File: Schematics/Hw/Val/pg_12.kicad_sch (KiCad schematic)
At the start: 19 parts, among them U1401 F04, U1402 F04, U1403 F04, U1404 F04, U1405 F04, U1406 F04, U1407 F04, U1408 F04, U1409 F04, U1410 F04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

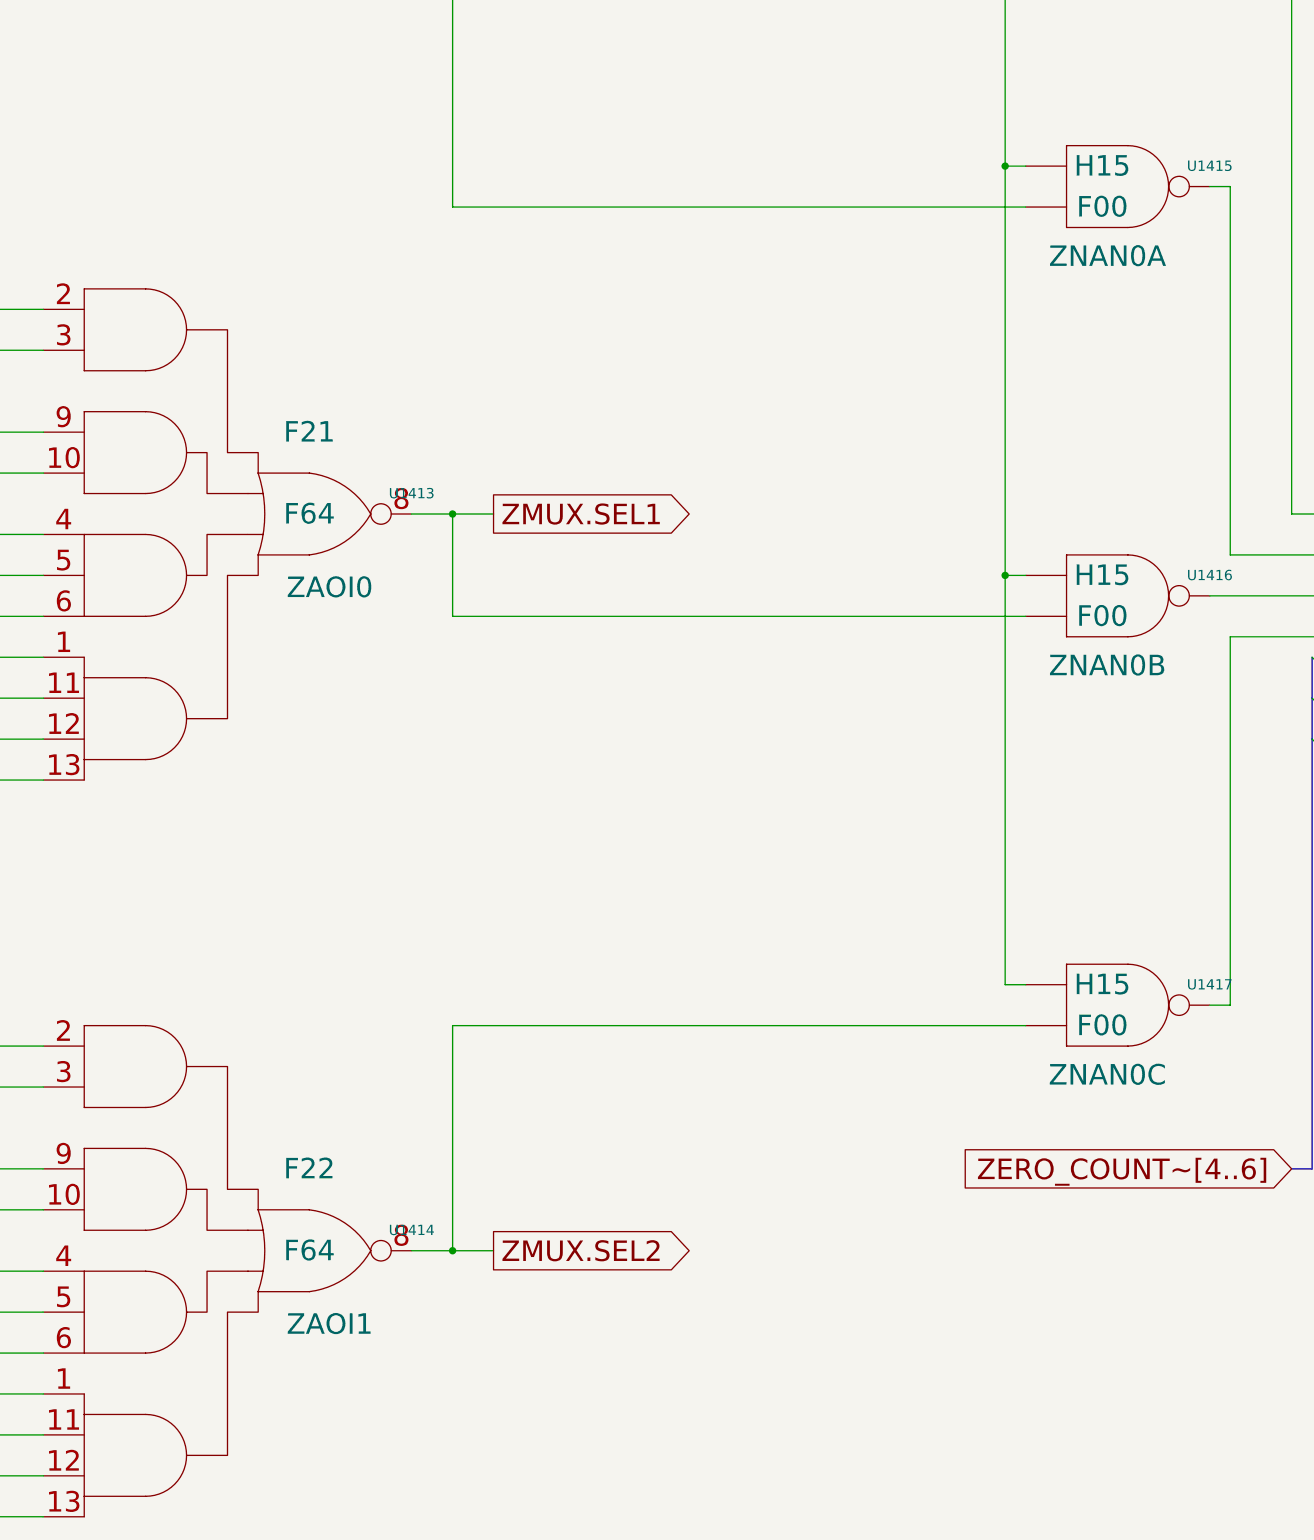
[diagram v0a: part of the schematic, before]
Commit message: Upgrade to KiCad9
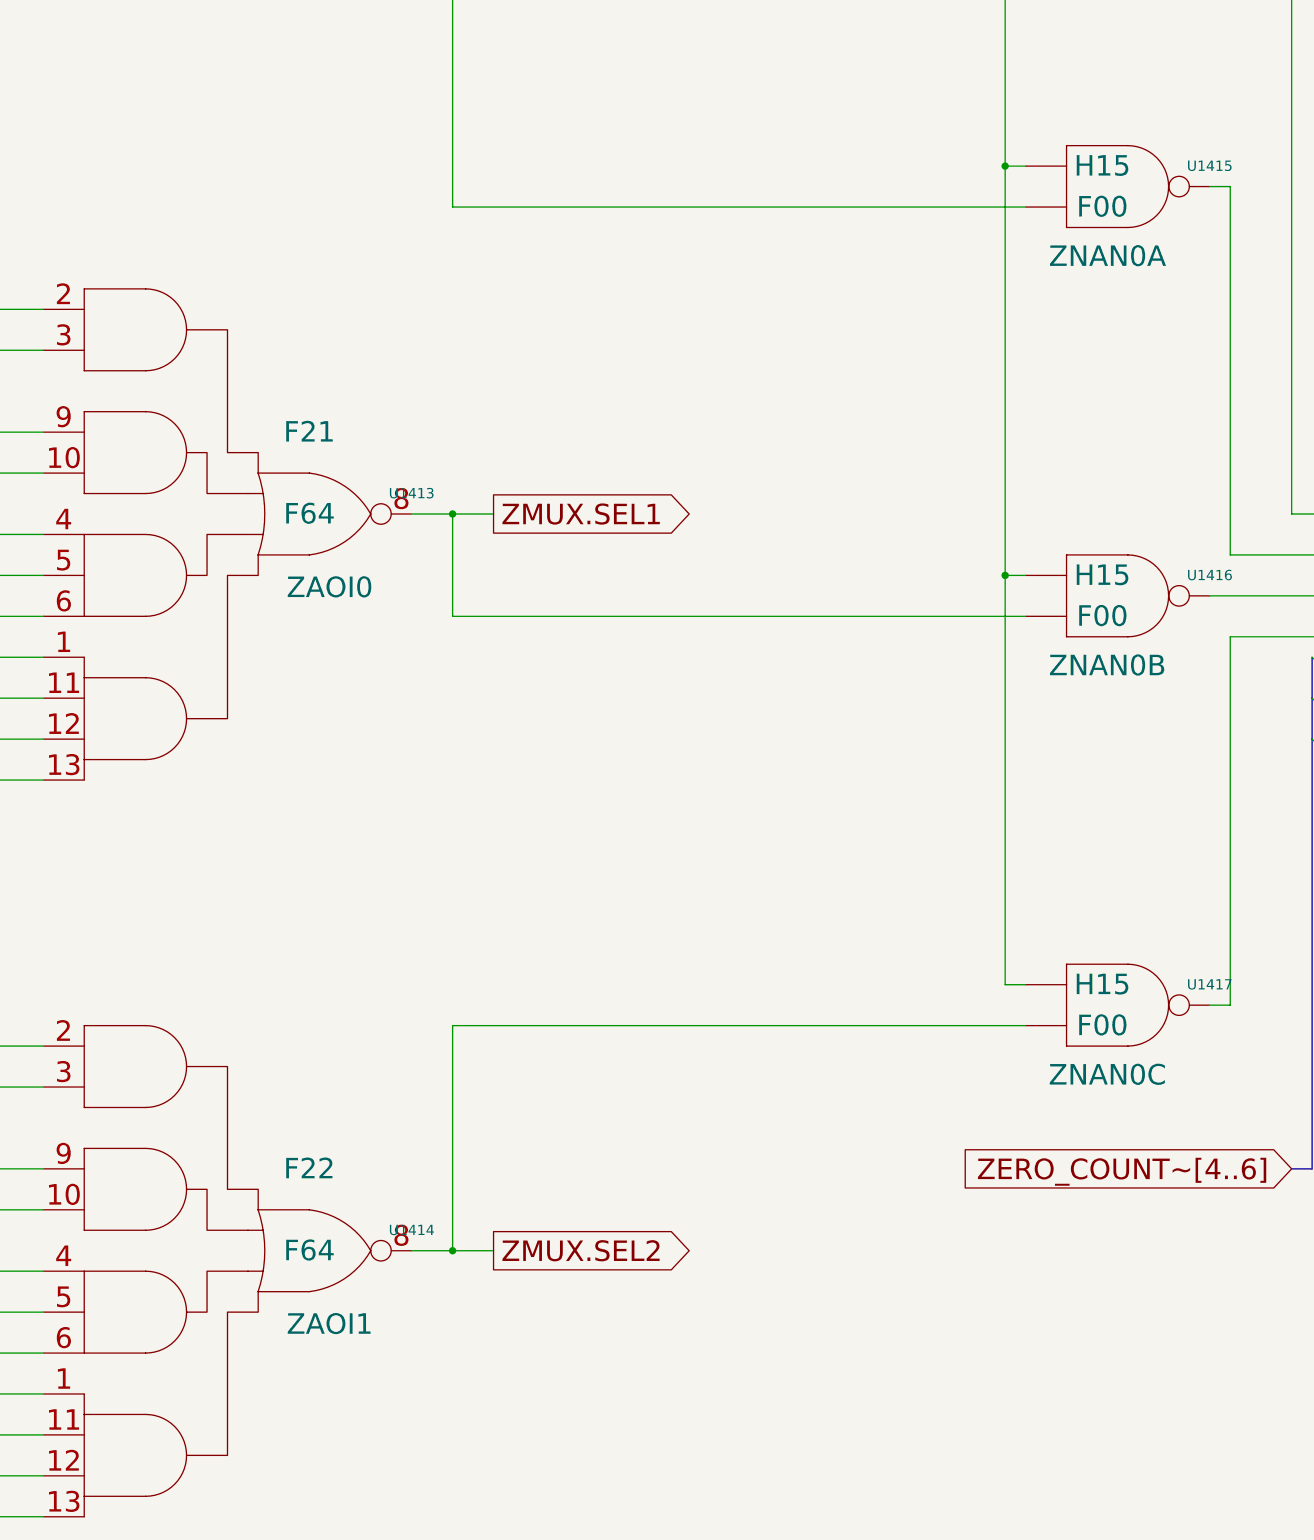
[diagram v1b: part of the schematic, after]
